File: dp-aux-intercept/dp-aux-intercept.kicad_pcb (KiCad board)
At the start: 2 copper layers, 0 parts

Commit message: Initial scatter.
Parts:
- added CCAN1: C, Capacitors_SMD:C_0805_HandSoldering, F.Cu at (94.1, 33.0)
- added CCAP1: C, Capacitors_SMD:C_0805_HandSoldering, F.Cu at (75.6, 46.2)
- added CDAN1: C, Capacitors_SMD:C_0805_HandSoldering, F.Cu at (67.4, 48.0)
- added CDAP1: C, Capacitors_SMD:C_0805_HandSoldering, F.Cu at (67.3, 54.3)
- added DPC1: DISPLAY_PORT, display_port:display_port, F.Cu at (31.0, 46.2)
- added DPD1: DISPLAY_PORT, display_port:display_port, B.Cu at (31.0, 26.9)
- added J1: CONN_02X03, Pin_Headers:Pin_Header_Straight_2x03, F.Cu at (57.6, 50.5)
- added J2: CONN_02X03, Pin_Headers:Pin_Header_Straight_2x03, F.Cu at (78.0, 29.6)
- added PAUX1: CONN_02X06, Pin_Headers:Pin_Header_Straight_2x06, F.Cu at (57.6, 30.1)
- added PCONF1: CONN_02X06, Pin_Headers:Pin_Header_Straight_2x06, F.Cu at (67.8, 30.1)
- added RCAN1: 100K, Resistors_SMD:R_0603_HandSoldering, F.Cu at (87.8, 38.7)
- added RCAN2: 50, Resistors_SMD:R_0603_HandSoldering, F.Cu at (72.7, 54.1)
- added RCAP1: 100K, Resistors_SMD:R_0603_HandSoldering, F.Cu at (80.9, 46.0)
- added RCAP2: 50, Resistors_SMD:R_0603_HandSoldering, F.Cu at (67.3, 60.4)
- added RCCFG1: 1M, Resistors_SMD:R_0603_HandSoldering, F.Cu at (94.6, 26.9)
- added RCCFG2: 5M, Resistors_SMD:R_0603_HandSoldering, F.Cu at (88.3, 32.8)
- added RCHPD1: 100K, Resistors_SMD:R_0603_HandSoldering, F.Cu at (72.1, 76.7)
- added RDAN1: 10K, Resistors_SMD:R_0603_HandSoldering, F.Cu at (93.2, 39.1)
- added RDAN2: 50, Resistors_SMD:R_0603_HandSoldering, F.Cu at (72.7, 60.0)
- added RDAP1: 10K, Resistors_SMD:R_0603_HandSoldering, F.Cu at (86.3, 46.0)
- added RDAP2: 50, Resistors_SMD:R_0603_HandSoldering, F.Cu at (80.9, 51.9)
- added RDCFG1: 1M, Resistors_SMD:R_0603_HandSoldering, F.Cu at (88.3, 26.9)
- added RDCFG2: 5M, Resistors_SMD:R_0603_HandSoldering, F.Cu at (47.3, 57.7)
- added RDHPD1: 100K, Resistors_SMD:R_0603_HandSoldering, F.Cu at (85.9, 68.8)

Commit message: Work on the PCB.
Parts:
- CCAN1, CDAN1, DPC1, J1, RCAN1, RCAN2, RDAN1, RDAN2: moved to B.Cu
- DPD1: moved to F.Cu
- moved RCCFG1 55.0 mm to (63.7, 72.4), turned to 180 degrees
- moved RCCFG2 44.4 mm to (65.0, 70.6), turned to 180 degrees
- moved RDAN1 39.7 mm to (59.9, 17.5), turned to 180 degrees
- moved J2 39.1 mm to (52.8, 59.5), turned to 90 degrees
- moved RDAP1 38.8 mm to (59.9, 17.5)
- moved PCONF1 38.8 mm to (52.8, 65.8), turned to 90 degrees
- moved RDCFG1 38.7 mm to (63.7, 56.8), turned to 180 degrees
- moved RDAN2 38.3 mm to (59.8, 23.9), turned to 180 degrees
- moved CCAN1 36.2 mm to (58.4, 39.0), turned to 270 degrees
- moved RDAP2 35.0 mm to (59.8, 23.9)
- moved CDAP1 34.7 mm to (58.6, 20.8), turned to 270 degrees
- moved DPC1 33.5 mm to (31.0, 79.8), turned to 180 degrees
- moved CDAN1 28.6 mm to (58.6, 20.8), turned to 270 degrees
- moved RCAN1 28.4 mm to (59.6, 42.2), turned to 180 degrees
- moved RCAP2 25.8 mm to (59.6, 35.8)
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
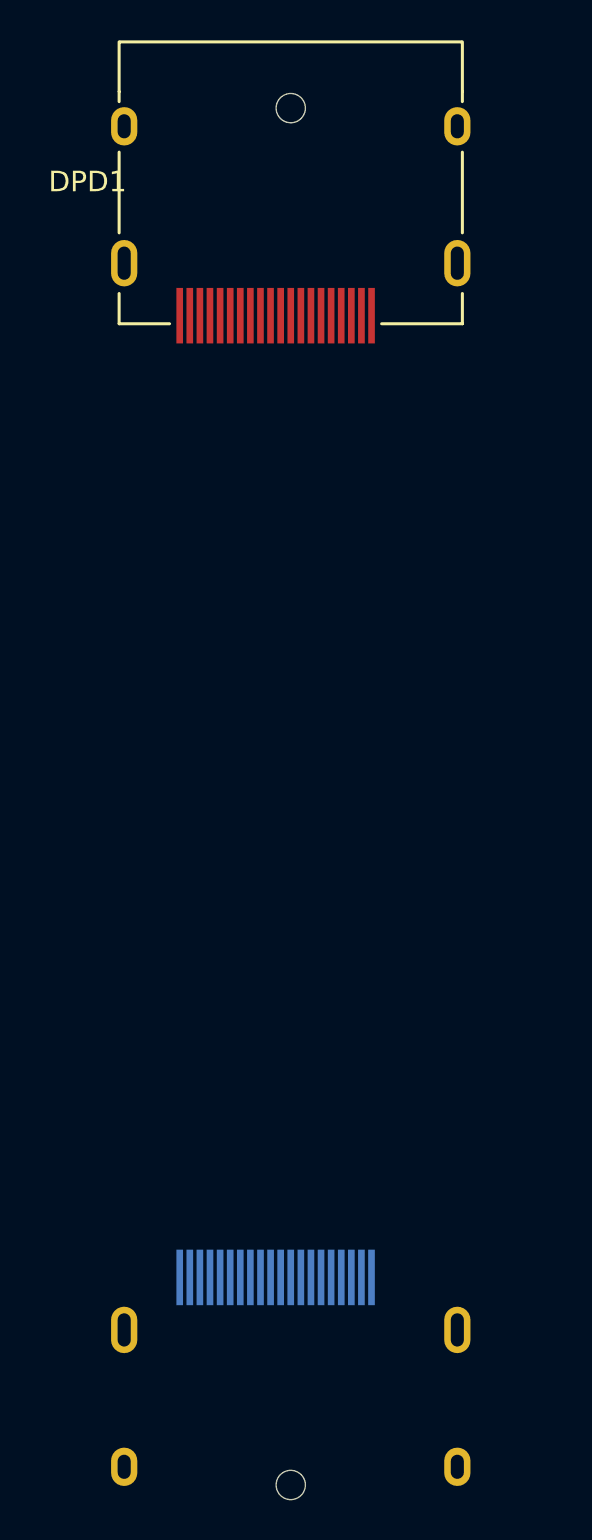
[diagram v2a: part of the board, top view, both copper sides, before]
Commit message: Changing to using the through-hole DisplayPort connectors.
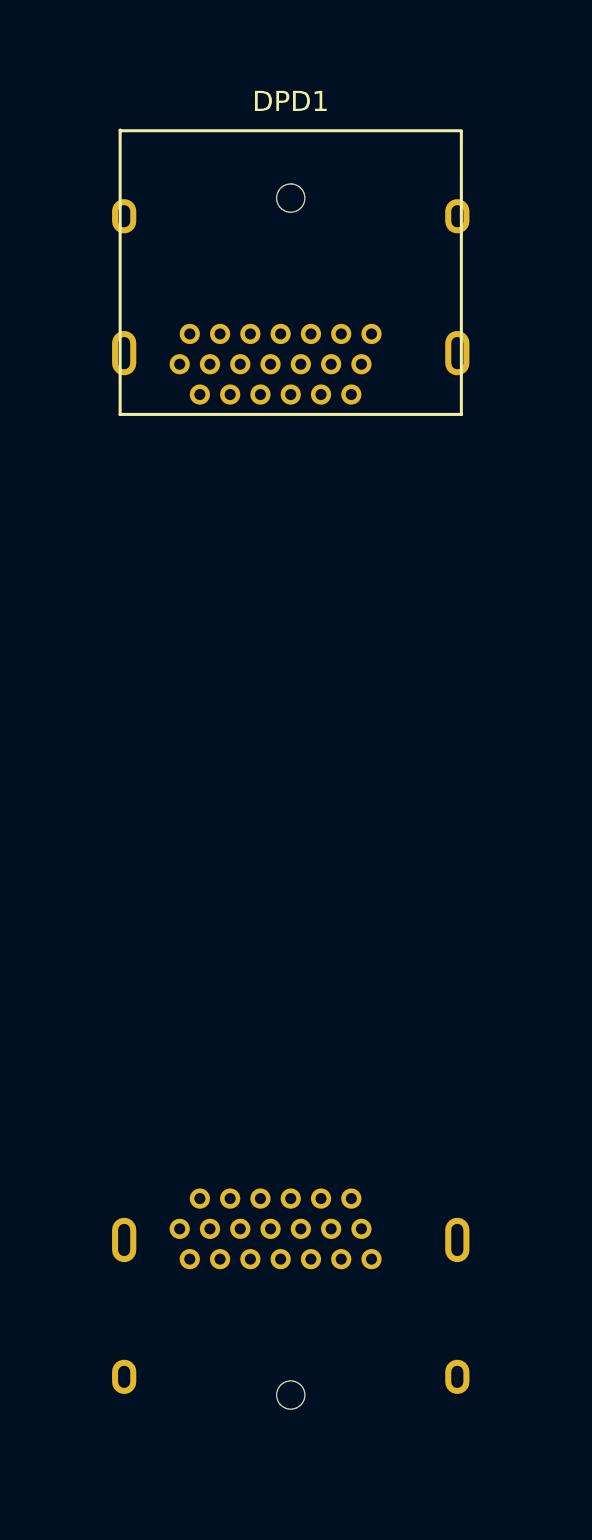
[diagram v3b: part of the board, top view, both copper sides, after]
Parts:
- DPC1, DPD1: footprint display_port:display_port -> 2040204-1:2040210-1

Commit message: Importing the updated netlist.
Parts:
- added PAUX1: CONN_02X06, Pin_Headers:Pin_Header_Straight_2x06, F.Cu at (76.8, 32.1)
- renumbered J1 to JCCFG1, J2 to JDCFG1, PAUX1 to PAUX2, PCONF1 to PCFG1
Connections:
- CCAN1 pad 1: /CAUX_RX_N -> Net-(CCAN1-Pad1)
- CCAP1 pad 1: /CAUX_RX_P -> Net-(CCAP1-Pad1)
- CDAN1 pad 2: /DAUX_RX_N -> Net-(CDAN1-Pad2)
- CDAP1 pad 2: /DAUX_RX_P -> Net-(CDAP1-Pad2)
- PAUX2 pad 1: /CAUX_RX_P -> /CAUX2_RX_P
- PAUX2 pad 2: /DAUX_RX_P -> /DAUX2_RX_P
- PAUX2 pad 3: /CAUX_RX_N -> /CAUX2_RX_N
- PAUX2 pad 4: /DAUX_RX_N -> /DAUX2_RX_N
- PAUX2 pad 5: /CAUX_RX_P -> /CAUX2_RX_P
- PAUX2 pad 6: /DAUX_RX_P -> /DAUX2_RX_P
- PAUX2 pad 7: /CAUX_RX_N -> /CAUX2_RX_N
- PAUX2 pad 8: /DAUX_RX_N -> /DAUX2_RX_N
- RCAN2 pad 2: /CAUX_RX_N -> Net-(CCAN1-Pad1)
- RCAP2 pad 1: /CAUX_RX_P -> Net-(CCAP1-Pad1)
- RDAN2 pad 2: /DAUX_RX_N -> Net-(CDAN1-Pad2)
- RDAP2 pad 1: /DAUX_RX_P -> Net-(CDAP1-Pad2)

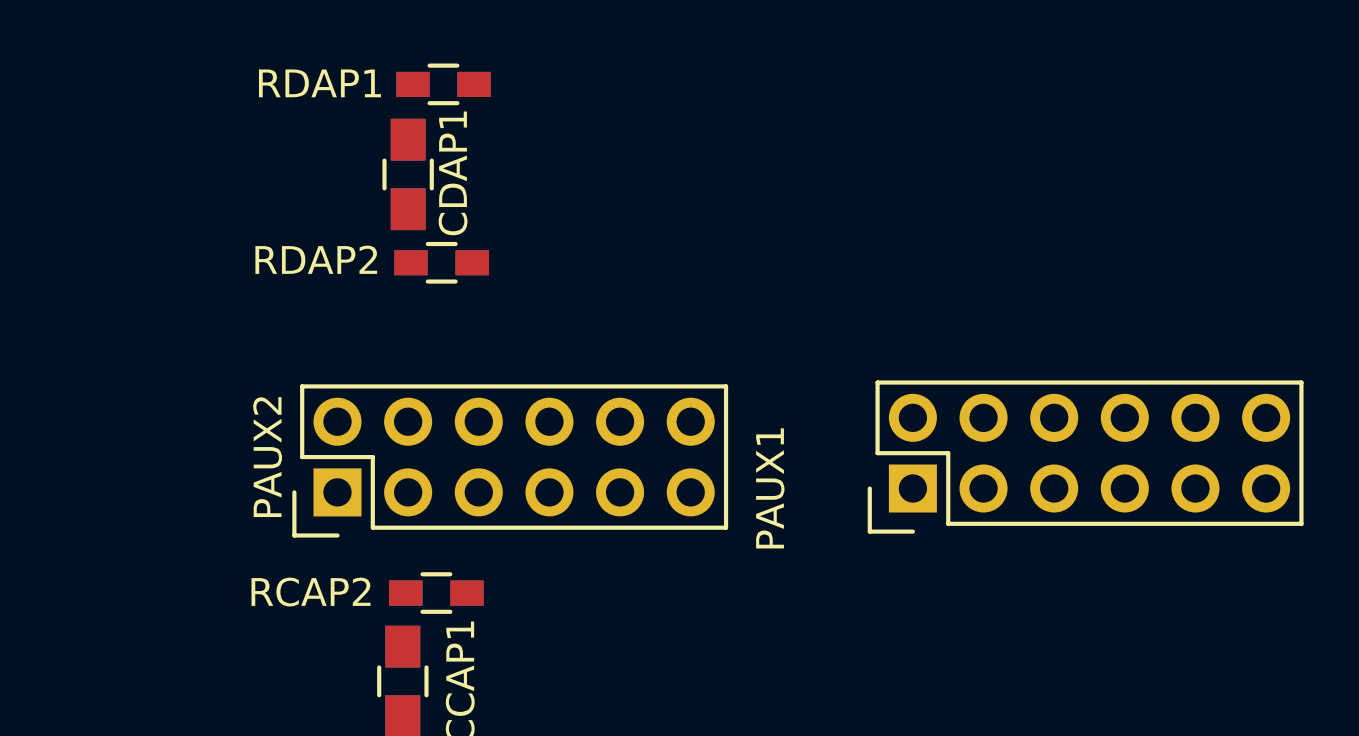
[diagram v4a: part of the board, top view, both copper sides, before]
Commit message: Changing the PAUX1 and PAUX2 to be right angle connectors.
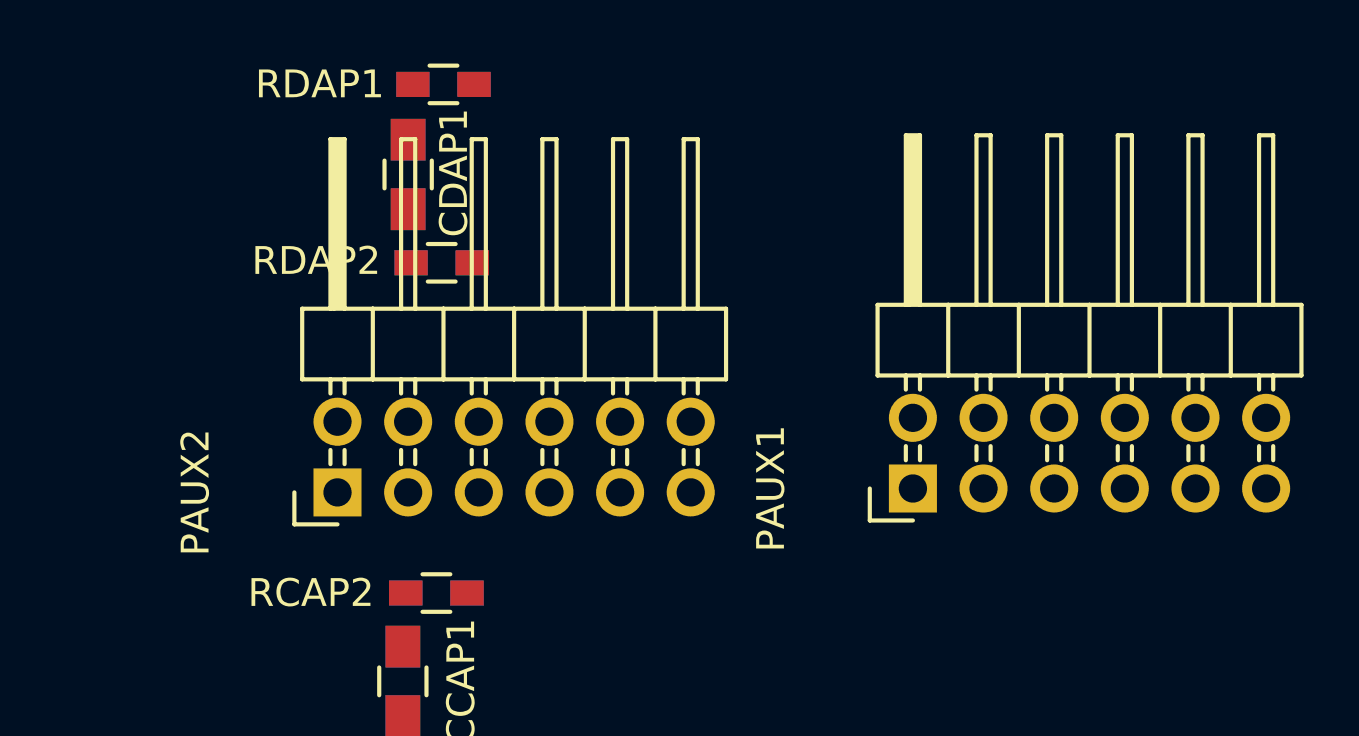
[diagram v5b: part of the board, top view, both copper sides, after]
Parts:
- PAUX1, PAUX2: footprint Pin_Headers:Pin_Header_Straight_2x06 -> Pin_Headers:Pin_Header_Angled_2x06

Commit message: Temp commit.
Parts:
- added JCAUXN1: CONN_01X03, Pin_Headers:Pin_Header_Straight_1x03, F.Cu at (105.8, 100.2)
- added JCAUXP1: CONN_01X03, Pin_Headers:Pin_Header_Straight_1x03, F.Cu at (102.2, 100.2)
- added JDAUXN1: CONN_01X03, Pin_Headers:Pin_Header_Straight_1x03, F.Cu at (109.3, 100.2)
- added JDAUXP1: CONN_01X03, Pin_Headers:Pin_Header_Straight_1x03, F.Cu at (112.9, 100.2)
- moved PAUX1 91.9 mm to (127.1, 109.0), turned to 0 degrees
- moved PAUX2 89.3 mm to (127.8, 85.5), turned to 0 degrees
- moved RCAN2 78.8 mm to (91.4, 107.9), turned to 90 degrees
- moved RCAP2 78.8 mm to (91.4, 107.9), turned to 270 degrees
- moved CCAN1 74.0 mm to (88.3, 106.7), turned to 180 degrees
- moved CCAP1 74.0 mm to (88.3, 106.7), turned to 180 degrees
- moved RCAN1 70.5 mm to (85.1, 107.9), turned to 90 degrees
- moved RCAP1 70.5 mm to (85.1, 107.9), turned to 270 degrees
- moved RDCFG1 27.9 mm to (36.8, 49.1), turned to 270 degrees
- moved RCCFG1 26.8 mm to (36.8, 72.1), turned to 90 degrees
- moved RDCFG2 26.7 mm to (40.0, 49.1), turned to 270 degrees
- moved RDHPD1 25.6 mm to (43.3, 49.1), turned to 270 degrees
- moved RCCFG2 25.0 mm to (40.0, 72.1), turned to 90 degrees
- moved RCHPD1 23.4 mm to (43.2, 72.1), turned to 90 degrees
- moved JCCFG1 15.7 mm to (37.5, 65.7)
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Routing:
- net GND: track 0.00 -> 20.7 mm, vias 0 -> 6
- net /DHPD: track 0.00 -> 15.3 mm
- net /CHPD: track 0.00 -> 14.0 mm
- net /DCFG2: track 0.00 -> 13.1 mm
- net /CCFG2: track 0.00 -> 11.7 mm
- net /DCFG1: track 0.00 -> 11.0 mm
- net /CCFG1: track 0.00 -> 8.69 mm
- net Net-(CCAN1-Pad1): track 0.00 -> 8.19 mm
- net Net-(CCAP1-Pad1): track 0.00 -> 4.93 mm
- net Net-(JCCFG1-Pad2): track 0.00 -> 3.06 mm
- net Net-(JDCFG1-Pad6): track 0.00 -> 3.06 mm
- net Net-(JDCFG1-Pad2): track 0.00 -> 3.06 mm
- net Net-(JCCFG1-Pad6): track 0.00 -> 3.01 mm
- net Net-(JCCFG1-Pad4): track 0.00 -> 2.80 mm
- net Net-(JDCFG1-Pad4): track 0.00 -> 2.80 mm
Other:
- net class Default: clearance 0.2 -> 0.15; trace_width 0.25 -> 0.15; via_drill 0.4 -> 0.3
- rule trace_clearance: 0.2 -> 0.15
- rule trace_min: 0.2 -> 0.15
- rule via_min_size: 0.4 -> 0.6

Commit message: Lots of updates to the PCB.
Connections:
- net Net-(CCAN1-Pad1) renamed /CAUX2_N
- net Net-(CCAP1-Pad1) renamed /CAUX2_P
- net Net-(CDAN1-Pad2) renamed /DAUX2_N
- net Net-(CDAP1-Pad2) renamed /DAUX2_P
- CCAN1 pad 2: /CAUX_N -> /CAUX1_N
- CCAP1 pad 2: /CAUX_P -> /CAUX1_P
- CDAN1 pad 1: /DAUX_N -> /DAUX1_N
- CDAP1 pad 1: /DAUX_P -> /DAUX1_P
- DPC1 pad 15: /CAUX_P -> /CAUX1_P
- DPC1 pad 17: /CAUX_N -> /CAUX1_N
- DPD1 pad 15: /DAUX_P -> /DAUX1_P
- DPD1 pad 17: /DAUX_N -> /DAUX1_N
- RCAN1 pad 2: /CAUX_N -> /CAUX1_N
- RCAP1 pad 1: /CAUX_P -> /CAUX1_P
- RDAN1 pad 2: /DAUX_N -> /DAUX1_N
- RDAP1 pad 1: /DAUX_P -> /DAUX1_P
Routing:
- net /ML2_N: track 0.00 -> 53.1 mm
- net /ML1_N: track 0.00 -> 53.1 mm
- net /ML2_P: track 0.00 -> 53.1 mm
- net /ML3_P: track 0.00 -> 53.1 mm
- net /ML1_P: track 0.00 -> 53.1 mm
- net /ML0_N: track 0.00 -> 52.7 mm
- net /ML0_P: track 0.00 -> 52.7 mm
- net /ML3_N: track 0.00 -> 50.3 mm
- net /CAUX1_N: track 0.00 -> 19.3 mm
- net /CAUX1_P: track 0.00 -> 16.8 mm
- net /DAUX1_N: track 0.00 -> 5.19 mm
- net /DAUX1_P: track 0.00 -> 4.94 mm

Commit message: Temp commit.
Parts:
- moved RCCFG2 121.6 mm to (161.2, 61.5)
- moved RDCFG2 121.6 mm to (161.2, 38.5)
- moved RCCFG1 121.6 mm to (158.0, 61.5)
- moved RDCFG1 121.6 mm to (158.0, 38.5)
- moved RDHPD1 121.6 mm to (164.5, 38.5)
- moved JCCFG1 121.6 mm to (158.7, 55.1)
- moved JDCFG1 121.6 mm to (158.7, 44.9)
- moved PCFG1 121.6 mm to (158.7, 51.2)
- moved RCHPD1 121.6 mm to (164.3, 61.5)
- moved RCAN1 61.5 mm to (33.5, 74.4), turned to 270 degrees
- moved RCAP1 61.5 mm to (33.5, 74.4), turned to 90 degrees
- moved CCAN1 60.3 mm to (36.7, 75.4)
- moved CCAP1 60.3 mm to (36.7, 75.4)
- moved RCAN2 60.3 mm to (39.9, 76.6)
- moved RCAP2 60.3 mm to (39.9, 76.6)
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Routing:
- net /DCFG1: track 11.0 -> 4.83 mm
- net /ML3_N: track 50.3 -> 53.1 mm
